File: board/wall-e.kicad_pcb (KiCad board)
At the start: 2 copper layers, 59 parts, among them J1 Raspberry_Pi_2_3, J10 PCA9685, J11 VL53L0X, J12 VL53L0X, J13 VL53L0X, J14 MotorDrv2, J15 Motor2, J16 IMU, J17 INA219, J18 INA219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

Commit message: Commit libraries and clean up.
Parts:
- moved C5 69.5 mm to (39.4, 27.9), turned to 90 degrees
- moved U1 59.9 mm to (67.3, 38.1), turned to 0 degrees
- moved J2 54.0 mm to (39.4, 38.1), turned to 270 degrees
- moved C2 43.7 mm to (124.5, 92.7)
- moved R10 43.7 mm to (92.7, 90.2)
- moved R11 43.7 mm to (92.7, 85.1)
- moved R13 43.7 mm to (92.7, 73.7)
- moved R14 43.7 mm to (92.7, 67.3)
- moved R9 43.7 mm to (92.7, 96.5)
- moved C10 43.7 mm to (120.7, 73.7)
- moved C11 43.7 mm to (119.4, 86.4)
- moved C13 43.7 mm to (156.2, 102.9)
- moved C3 43.7 mm to (116.8, 96.5)
- moved C8 43.7 mm to (105.4, 82.5)
- moved C9 43.7 mm to (113.0, 72.4)
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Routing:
- net GND: track 0.00 -> 3.84 mm, vias 0 -> 1
- added copper zone on B.Cu, net GND

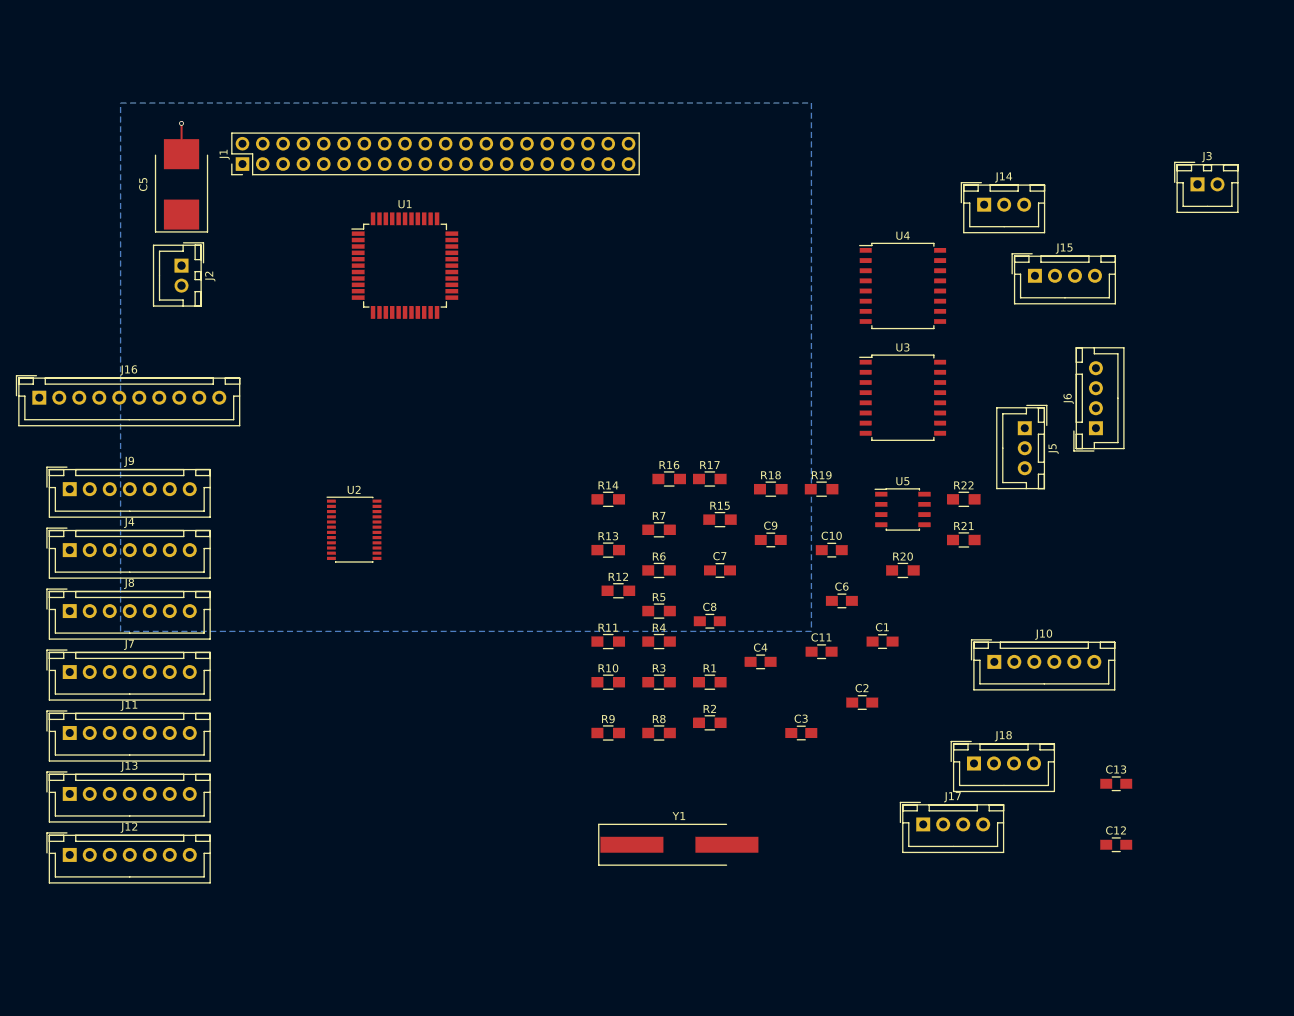
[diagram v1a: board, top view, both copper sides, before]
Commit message: Start to group components on board.
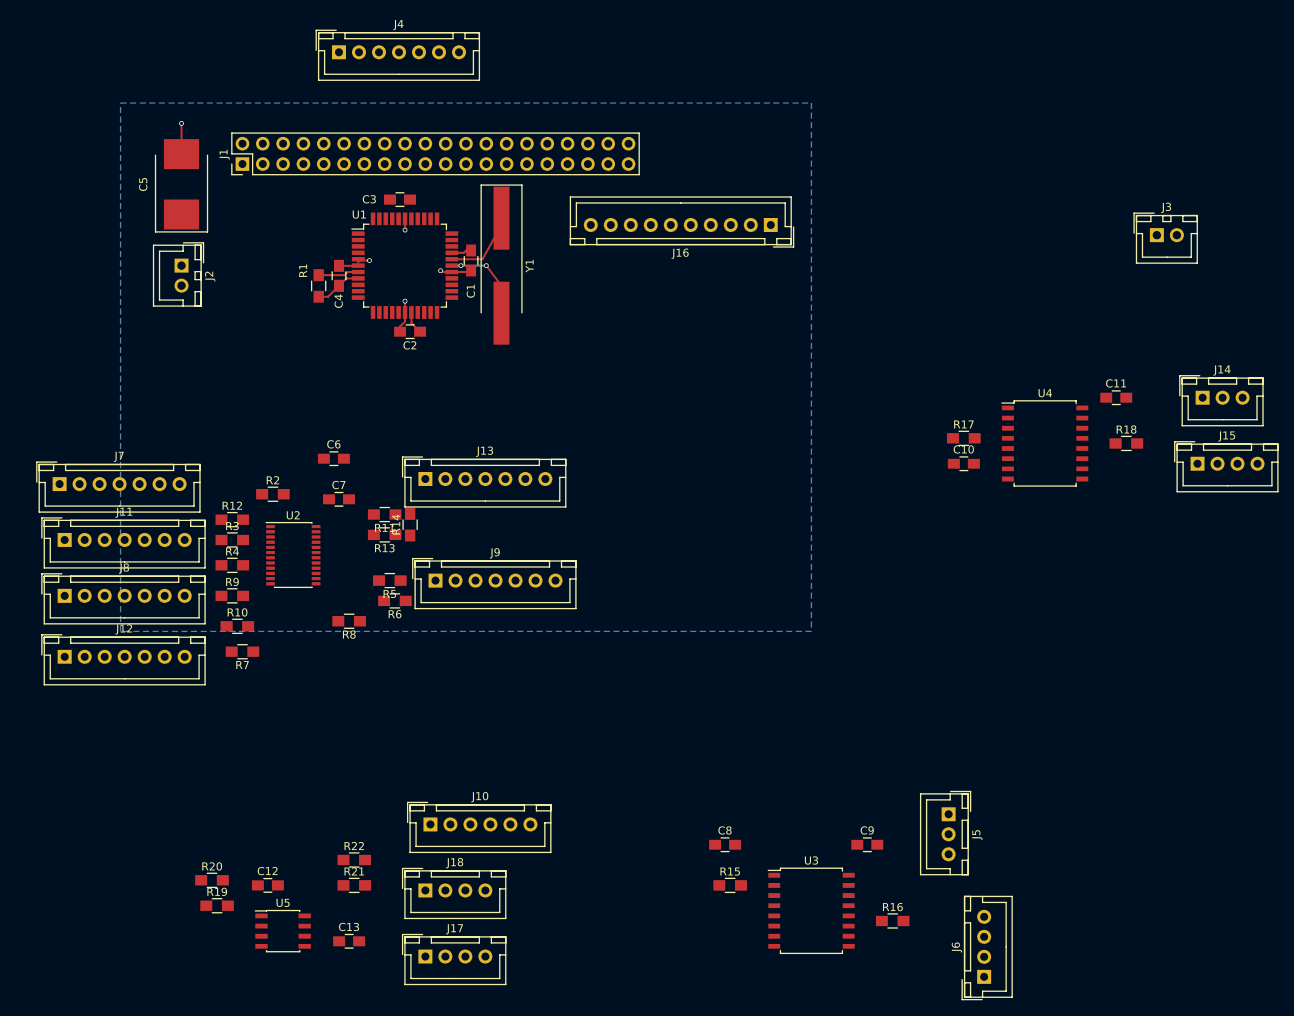
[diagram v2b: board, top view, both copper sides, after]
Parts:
- moved C12 106.2 mm to (50.2, 115.6)
- moved C13 97.9 mm to (60.3, 122.6)
- moved R20 94.6 mm to (43.2, 114.9)
- moved J16 94.0 mm to (113.0, 33.0), turned to 180 degrees
- moved U5 93.7 mm to (52.1, 121.3)
- moved R19 91.8 mm to (43.8, 118.1)
- moved R22 88.5 mm to (61.0, 112.4)
- moved R21 87.6 mm to (61.0, 115.6)
- moved C3 83.4 mm to (66.7, 29.8)
- moved Y1 75.7 mm to (79.4, 38.1), turned to 270 degrees
- moved J10 73.4 mm to (70.5, 108.0)
- moved C2 73.1 mm to (67.9, 46.4), turned to 180 degrees
- moved C4 71.5 mm to (59.1, 39.4), turned to 90 degrees
- moved J4 70.7 mm to (59.1, 11.4)
- moved J18 70.4 mm to (69.8, 116.2)
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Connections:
- C12 pad 2: Net-(C12-Pad2) -> GND
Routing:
- net GND: track 3.84 -> 18.0 mm, vias 1 -> 5
- net +3V3: track 0.00 -> 11.3 mm
- net Net-(U1-Pad28): track 0.00 -> 10.9 mm, vias 0 -> 2
- net Net-(U1-Pad29): track 0.00 -> 9.59 mm
- net PROP_RES: track 0.00 -> 5.11 mm

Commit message: Do some routing
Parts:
- moved R6 48.6 mm to (20.3, 63.5), turned to 0 degrees
- moved R13 46.2 mm to (20.3, 84.3), turned to 0 degrees
- moved R7 28.1 mm to (20.3, 77.5), turned to 0 degrees
- moved R10 26.5 mm to (20.3, 88.1)
- moved R9 26.0 mm to (20.3, 73.9)
- moved R3 26.0 mm to (20.3, 67.1)
- moved R4 25.9 mm to (20.3, 80.8)
- moved J2 25.9 mm to (20.3, 20.6)
- moved R12 25.4 mm to (20.3, 70.4)
- moved C5 22.0 mm to (19.1, 36.3)
- moved C3 20.3 mm to (53.1, 45.0), turned to 90 degrees
- moved Y1 19.2 mm to (61.3, 31.5), turned to 0 degrees
- moved R1 15.6 mm to (63.9, 54.4), turned to 180 degrees
- moved C1 15.0 mm to (60.7, 35.3), turned to 0 degrees
- moved C4 12.9 mm to (62.6, 51.8), turned to 180 degrees
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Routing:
- net +5V: track 0.00 -> 39.6 mm
- net I2C_M3_SCLK: track 0.00 -> 32.5 mm
- net I2C_M0_SCLK: track 0.00 -> 31.6 mm
- net I2C_M0_SDA: track 0.00 -> 31.0 mm
- net I2C_M3_SDA: track 0.00 -> 30.7 mm
- net I2C_M2_SCLK: track 0.00 -> 27.1 mm
- net I2C_M1_SDA: track 0.00 -> 25.4 mm
- net I2C_M1_SCLK: track 0.00 -> 25.2 mm
- net I2C_M2_SDA: track 0.00 -> 25.2 mm
- net +3V3: track 11.3 -> 18.3 mm
- net Net-(R2-Pad1): track 0.00 -> 6.68 mm
- net GND: track 18.0 -> 21.4 mm, vias 5 -> 7

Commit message: More routing; add Pi outline.
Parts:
- added REF**: MountingHole_2.7mm_M2.5, Mounting_Holes:MountingHole_2.7mm_M2.5, F.Cu at (17.3, 17.3)
- added REF**: MountingHole_2.7mm_M2.5, Mounting_Holes:MountingHole_2.7mm_M2.5, F.Cu at (17.3, 66.3)
- added REF**: MountingHole_2.7mm_M2.5, Mounting_Holes:MountingHole_2.7mm_M2.5, F.Cu at (75.3, 17.3)
- added REF**: MountingHole_2.7mm_M2.5, Mounting_Holes:MountingHole_2.7mm_M2.5, F.Cu at (75.3, 66.3)
- C1, C2, C3, C4: moved to B.Cu
- moved C3 246.2 mm to (290.1, 111.8)
- moved C1 243.4 mm to (292.9, 108.3)
- moved U1 241.9 mm to (293.5, 111.4)
- moved R1 241.9 mm to (296.0, 122.2)
- moved Y1 240.6 mm to (291.6, 101.3)
- moved C4 239.7 mm to (294.0, 114.5)
- moved C2 237.0 mm to (296.6, 111.0)
- moved C8 191.7 mm to (295.3, 148.0), turned to 270 degrees
- moved R15 186.4 mm to (291.0, 150.5)
- moved R10 186.3 mm to (206.1, 102.0), turned to 90 degrees
- moved R13 182.8 mm to (202.3, 102.0), turned to 90 degrees
- moved R4 179.7 mm to (198.7, 102.0), turned to 90 degrees
- moved J12 178.5 mm to (204.3, 95.5), turned to 90 degrees
- moved R7 176.8 mm to (195.4, 102.0), turned to 90 degrees
- moved R9 173.8 mm to (191.9, 102.0), turned to 90 degrees
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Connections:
- C7 pad 2: Net-(C7-Pad2) -> GND
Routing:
- net +5V: track 39.6 -> 102.2 mm
- net +3V3: track 18.3 -> 69.3 mm, vias 0 -> 4
- net +5VP: track 0.00 -> 42.7 mm
- net I2C_M4_SDA: track 0.00 -> 41.2 mm
- net I2C_M4_SCLK: track 0.00 -> 40.1 mm
- net PI_SPI_CE1: track 0.00 -> 33.0 mm
- net PI_I2C_SCLK: track 0.00 -> 21.9 mm
- net PI_I2C_SDA: track 0.00 -> 21.1 mm
- net PI_SPI_SCLK: track 0.00 -> 18.2 mm
- net SCREEN_RST: track 0.00 -> 16.6 mm
- net PI_SPI1_MISO: track 0.00 -> 15.5 mm
- net Net-(J5-Pad2): track 0.00 -> 14.2 mm
- net Net-(R15-Pad1): track 0.00 -> 12.6 mm
- net PI_SPI1_SCLK: track 0.00 -> 12.4 mm
- net Net-(J6-Pad3): track 0.00 -> 11.4 mm
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- added copper zone on B.Cu, net GNDA
- added copper zone on F.Cu, net GNDA

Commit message: Pi outline
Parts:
- REF** (x4): value MountingHole_2.7mm_M2.5 -> M2.5
- moved C1 168.6 mm to (129.6, 150.3)
- moved J12 168.6 mm to (41.1, 137.5)
- moved J3 168.6 mm to (123.5, 105.4)
- moved J7 168.6 mm to (20.1, 137.5)
- moved R10 168.6 mm to (42.8, 144.0)
- moved R11 168.6 mm to (36.0, 105.0)
- moved R12 168.6 mm to (25.1, 144.0)
- moved R13 168.6 mm to (39.0, 144.0)
- moved R15 168.6 mm to (127.8, 192.5)
- moved R18 168.6 mm to (133.4, 118.8)
- moved R3 168.6 mm to (21.8, 144.0)
- moved R4 168.6 mm to (35.5, 144.0)
- moved R6 168.6 mm to (18.2, 144.0)
- moved R7 168.6 mm to (32.2, 144.0)
- moved R9 168.6 mm to (28.6, 144.0)
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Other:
- board text added: "Camera"
- board text added: "Ethernet and USB ports"

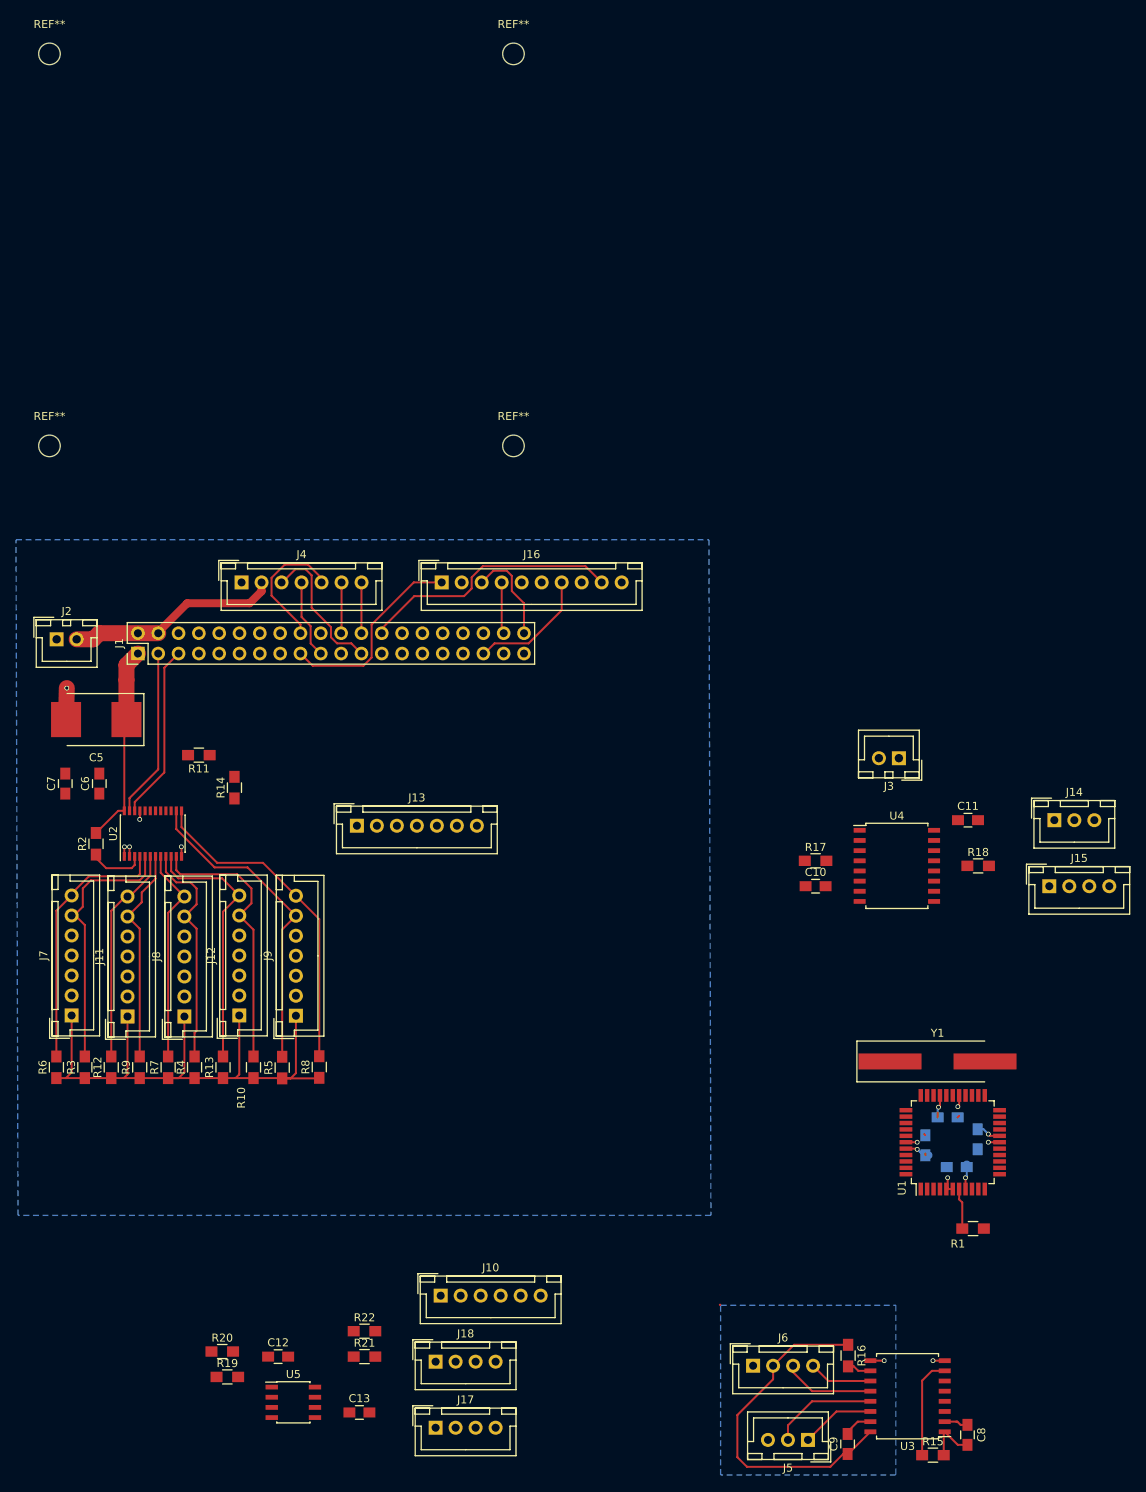
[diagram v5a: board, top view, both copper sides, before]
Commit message: Smaller board
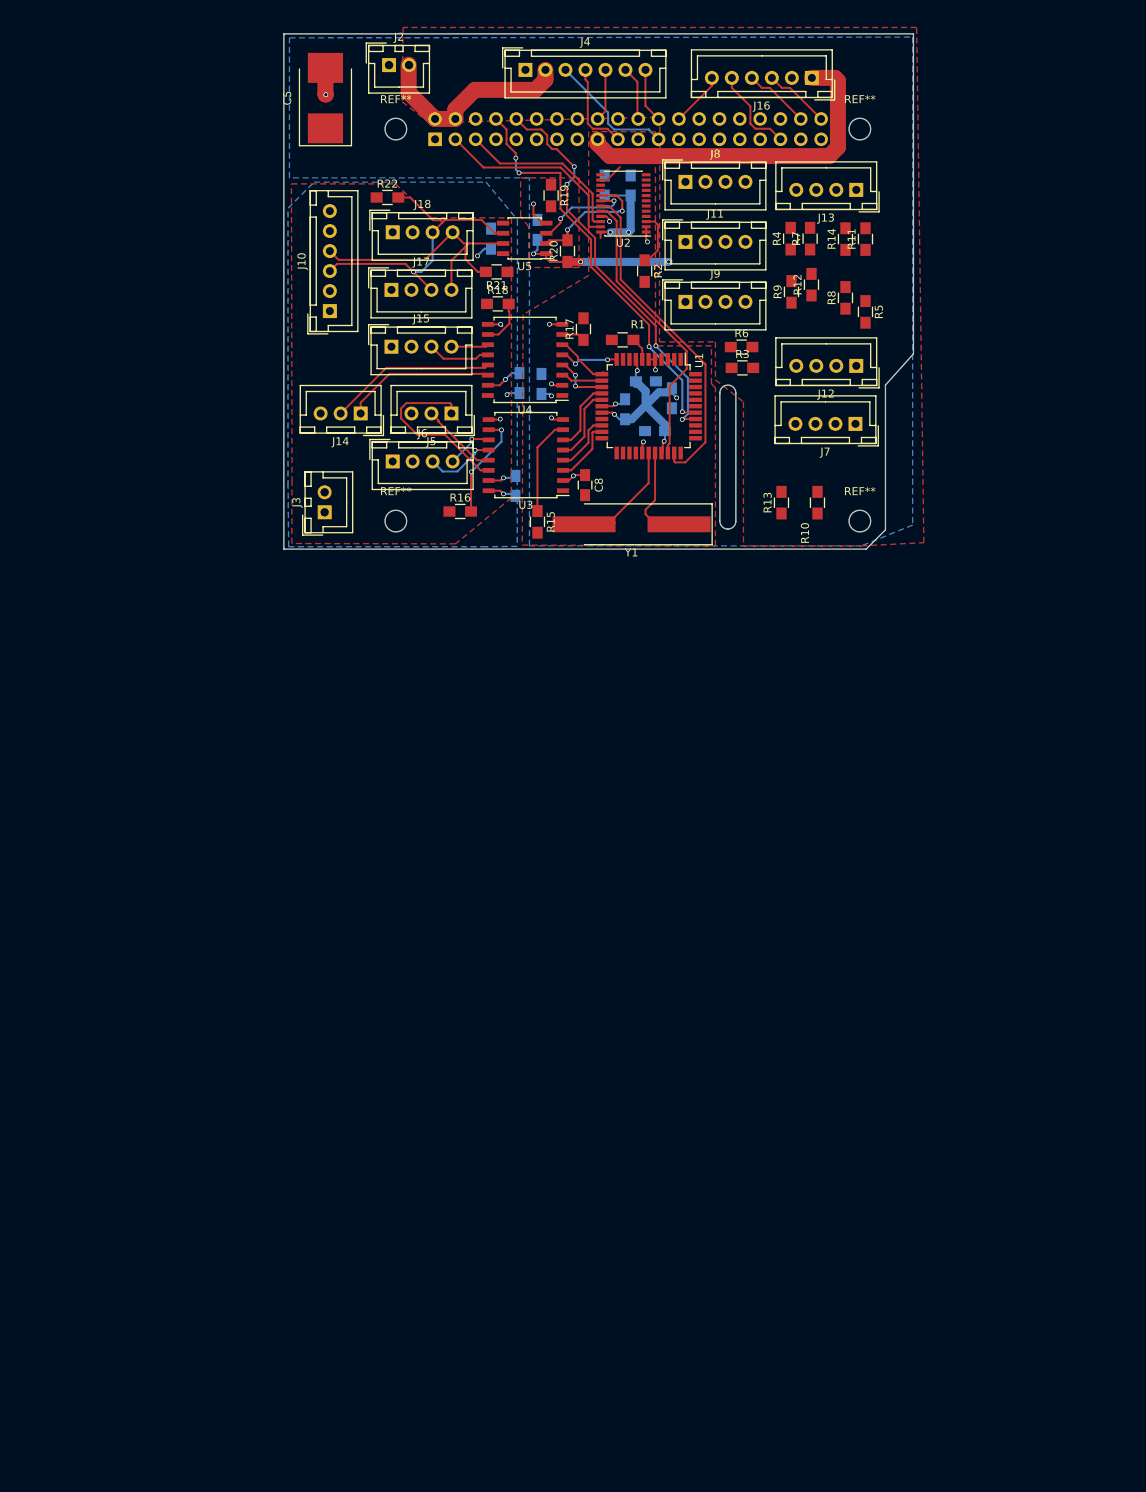
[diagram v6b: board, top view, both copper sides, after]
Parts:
- C10, C11, C12, C13, C6, C7, C9: moved to B.Cu
- J1: footprint Pin_Headers:Pin_Header_Straight_2x20_Pitch2.54mm -> Socket_Strips:Socket_Strip_Straight_2x20_Pitch2.54mm; moved to B.Cu
- J11, J12, J13, J7, J8, J9: footprint Connectors_JST:JST_XH_B07B-XH-A_07x2.50mm_Straight -> Connectors_JST:JST_XH_B04B-XH-A_04x2.50mm_Straight
- J16: footprint Connectors_JST:JST_XH_B10B-XH-A_10x2.50mm_Straight -> Connectors_JST:JST_XH_B06B-XH-A_06x2.50mm_Straight
- moved R19 153.1 mm to (80.0, 35.0), turned to 270 degrees
- moved U5 148.3 mm to (76.7, 40.4), turned to 180 degrees
- moved C13 147.6 mm to (72.5, 40.4), turned to 90 degrees
- moved C12 144.5 mm to (78.3, 39.3), turned to 90 degrees
- moved R20 144.2 mm to (82.1, 42.0), turned to 90 degrees
- moved J17 142.3 mm to (60.1, 46.8)
- moved R22 141.7 mm to (59.6, 35.3)
- moved J18 141.3 mm to (60.2, 39.6)
- moved R21 136.6 mm to (73.2, 44.6), turned to 180 degrees
- moved J5 135.8 mm to (67.6, 62.3)
- moved R12 131.3 mm to (112.6, 46.2)
- moved R7 131.0 mm to (112.4, 40.4)
- moved C8 128.0 mm to (84.3, 71.2)
- moved R4 127.6 mm to (110.0, 40.4)
- moved U3 126.9 mm to (76.9, 67.5)
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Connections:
- C11 pad 2: Net-(C11-Pad2) -> GNDA
- C9 pad 2: Net-(C9-Pad2) -> GNDA
- J11 pad 2: Net-(J11-Pad2) -> GND
- J11 pad 3: GND -> I2C_M1_SCLK
- J11 pad 4: Net-(J11-Pad4) -> I2C_M1_SDA
- J12 pad 2: Net-(J12-Pad2) -> GND
- J12 pad 3: GND -> I2C_M3_SCLK
- J12 pad 4: Net-(J12-Pad4) -> I2C_M3_SDA
- J13 pad 2: Net-(J13-Pad2) -> GND
- J13 pad 3: GND -> I2C_M5_SCLK
- J13 pad 4: Net-(J13-Pad4) -> I2C_M5_SDA
- J16 pad 5: Net-(J16-Pad5) -> PI_SPI1_MISO
- J16 pad 6: Net-(J16-Pad6) -> PI_SPI_CE1
- J7 pad 2: Net-(J7-Pad2) -> GND
- J7 pad 3: GND -> I2C_M0_SCLK
- J7 pad 4: Net-(J7-Pad4) -> I2C_M0_SDA
- J8 pad 2: Net-(J8-Pad2) -> GND
- J8 pad 3: GND -> I2C_M2_SCLK
- J8 pad 4: Net-(J8-Pad4) -> I2C_M2_SDA
- J9 pad 2: Net-(J9-Pad2) -> GND
- J9 pad 3: GND -> I2C_M4_SCLK
- J9 pad 4: Net-(J9-Pad4) -> I2C_M4_SDA
- U3 pad 15: Net-(C9-Pad2) -> GNDA
- U3 pad 3: M1_DIR -> M3_DIR
- U3 pad 4: M1_PWM -> M3_PWM
- U3 pad 5: M1_ENCA -> M3_ENCA
- U3 pad 6: M1_ENCB -> M3_ENCB
- U4 pad 15: Net-(C11-Pad2) -> GNDA
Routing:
- net +5V: track 102.2 -> 45.5 mm, vias 0 -> 3
- net PI_TX: track 0.00 -> 51.0 mm, vias 0 -> 4
- net PI_RX: track 0.25 -> 50.5 mm, vias 0 -> 4
- net I2C_M7_SDA: track 0.00 -> 41.6 mm
- net I2C_M4_SDA: track 41.2 -> 0.00 mm
- net I2C_ISO_SCL: track 0.00 -> 37.9 mm, vias 0 -> 1
- net I2C_M4_SCLK: track 40.1 -> 3.09 mm
- net I2C_M7_SCLK: track 0.00 -> 36.1 mm
- net I2C_ISO_SDA: track 0.00 -> 35.6 mm
- net +5VP: track 42.7 -> 7.57 mm, vias 0 -> 3
- net I2C_M3_SCLK: track 34.4 -> 0.00 mm
- net I2C_M0_SCLK: track 33.5 -> 0.21 mm
- net I2C_M3_SDA: track 32.6 -> 0.00 mm
- net I2C_M0_SDA: track 32.9 -> 0.49 mm
- net I2C_M2_SCLK: track 29.0 -> 0.00 mm
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- added copper zone on F.Cu, net +3V3
- added copper zone on F.Cu, net +5V
- added copper zone on F.Cu, net +5VP
- removed copper zone on F.Cu, net GNDA
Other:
- board outline added: 78.7 x 64.4 mm
- net class Default: clearance 0.2 -> 0.25
- rule trace_clearance: 0.2 -> 0.25

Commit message: Routed
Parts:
- moved R10 25.2 mm to (119.8, 49.0), turned to 180 degrees
- moved R13 24.8 mm to (122.3, 52.7), turned to 270 degrees
- moved J9 15.3 mm to (100.1, 33.3)
- moved R5 9.70 mm to (119.5, 39.9), turned to 90 degrees
- moved R8 9.45 mm to (121.9, 39.9)
- moved J8 7.59 mm to (99.1, 40.6)
- moved J11 7.12 mm to (99.1, 47.6)
- moved R14 6.06 mm to (120.5, 45.3)
- moved R11 4.90 mm to (118.3, 45.3)
- moved R3 3.64 mm to (104.8, 53.0)
- moved R12 2.96 mm to (112.8, 49.1), turned to 180 degrees
- moved J13 2.90 mm to (121.1, 34.3)
- moved R9 2.80 mm to (112.8, 46.3), turned to 180 degrees
- moved R7 2.34 mm to (112.0, 42.7), turned to 180 degrees
- moved R4 2.00 mm to (112.0, 40.3), turned to 180 degrees
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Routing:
- net +3V3: track 83.6 -> 179.4 mm, vias 7 -> 11
- net I2C_M3_SDA: track 0.00 -> 59.8 mm
- net I2C_M5_SDA: track 0.00 -> 49.4 mm
- net I2C_M3_SCLK: track 0.00 -> 48.3 mm
- net I2C_M4_SDA: track 0.00 -> 46.5 mm
- net I2C_M5_SCLK: track 0.00 -> 45.4 mm
- net I2C_M4_SCLK: track 3.09 -> 48.3 mm
- net I2C_M0_SCLK: track 0.21 -> 40.5 mm
- net I2C_M0_SDA: track 0.49 -> 38.1 mm
- net I2C_M1_SDA: track 0.00 -> 31.0 mm
- net I2C_M1_SCLK: track 0.00 -> 28.5 mm
- net +5V: track 45.5 -> 70.6 mm, vias 3 -> 6
- net I2C_M2_SDA: track 0.00 -> 24.7 mm
- net I2C_M2_SCLK: track 0.00 -> 22.2 mm
- net I2C_M7_SCLK: track 36.1 -> 41.8 mm
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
